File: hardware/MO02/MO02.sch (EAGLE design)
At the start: 28 parts, among them J1 AUDIO-JACK2PTH, J2 M04X2, Q1 G2XX3---PW20, Q4 32.768 kHz, SW1 DTS-6

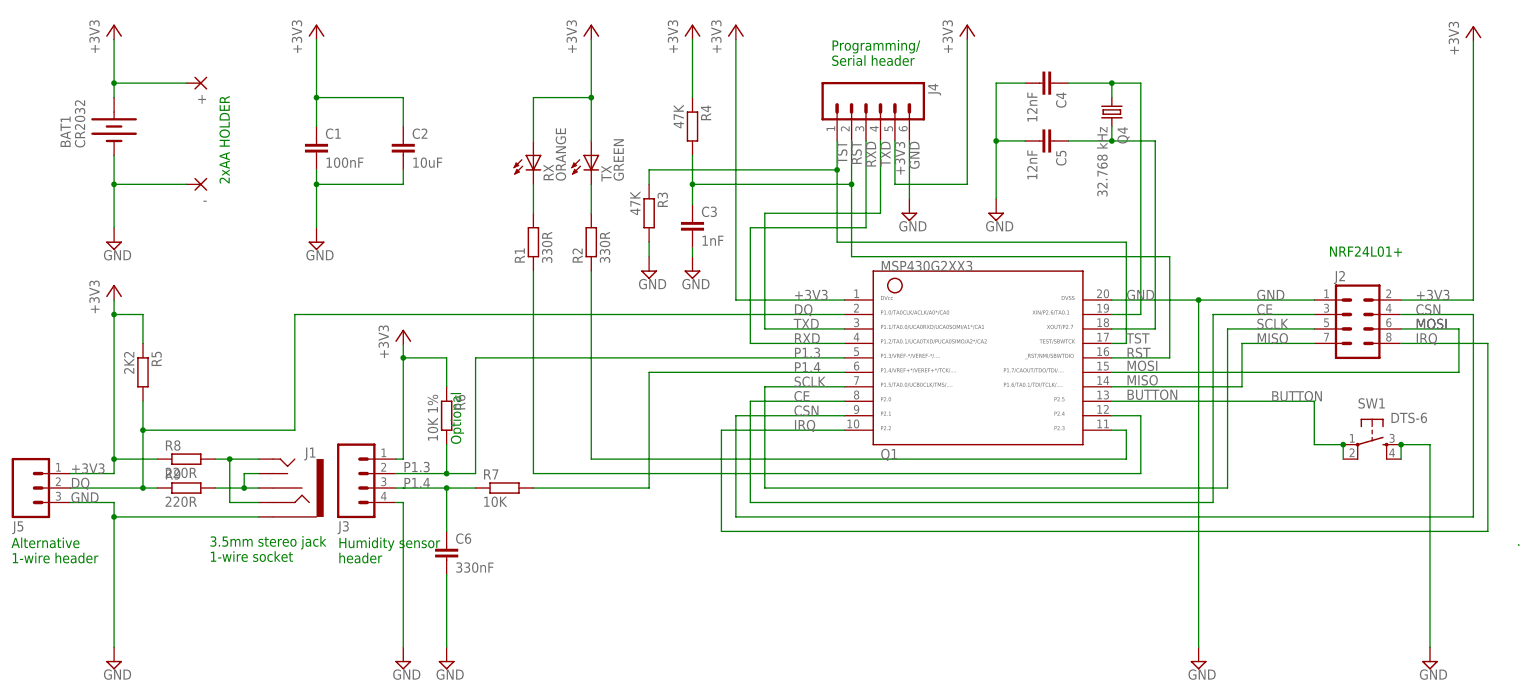
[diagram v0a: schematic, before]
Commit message: 2x6mm watch crystal, isolated ground plane, no external caps
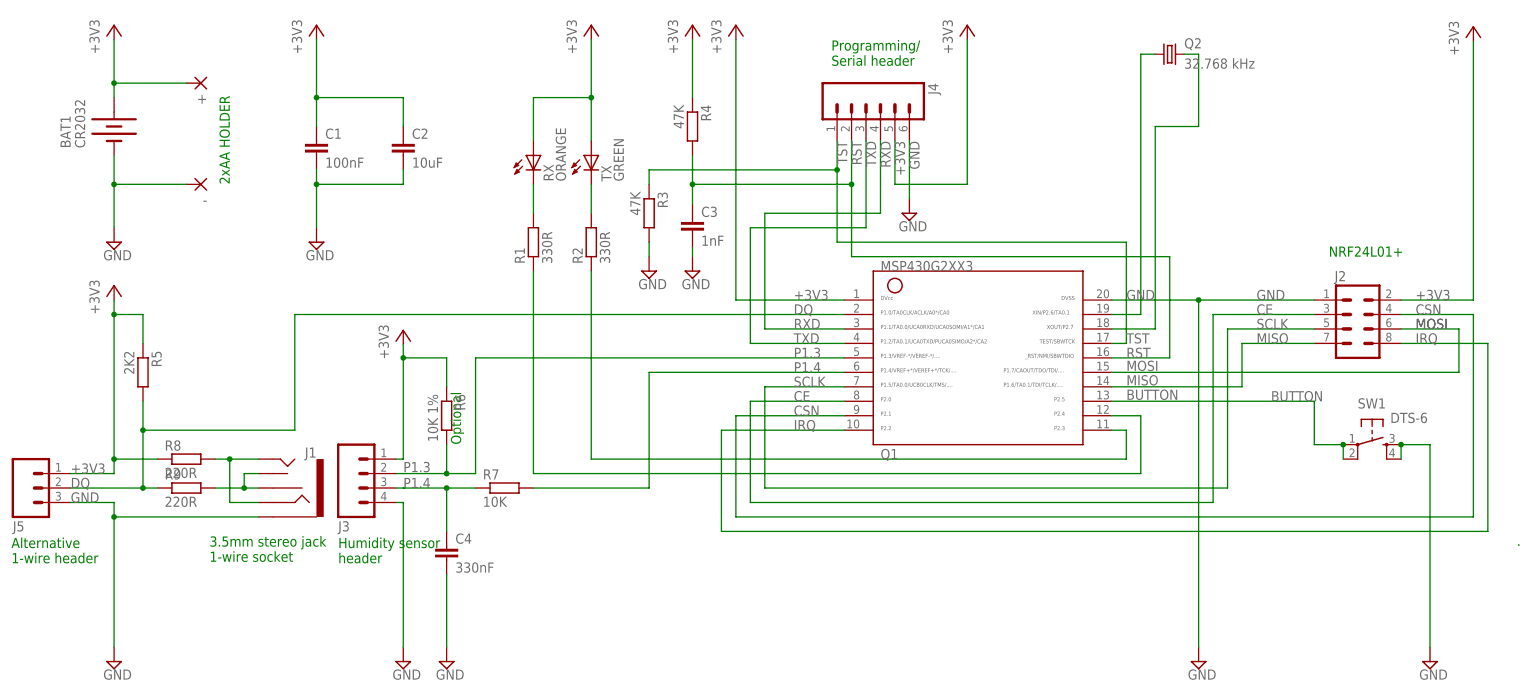
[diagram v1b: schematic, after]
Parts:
- removed C5: 12nF, resistor:C-EUC0805
- removed C6: 330nF, resistor:C-EUC0805
- removed Q4: 32.768 kHz, crystal:CRYSTALTC38H
- added Q2: 32.768 kHz, crystal:CRYSTALTC26H
- C4: value 12nF -> 330nF
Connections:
- net GND: no longer C5.2, C6.2
- net N$7: now also C4.1; no longer C6.1
- net P2.6: now also Q2.1; no longer C4.1, Q4.1
- net P2.7: now also Q2.2; no longer C5.1, Q4.2
- net RXD: now also J4.4, Q1.3; no longer J4.3, Q1.4
- net TXD: now also J4.3, Q1.4; no longer J4.4, Q1.3
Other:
- moved on the sheet: C4
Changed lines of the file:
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@@
 <part name="BAT1" library="SparkFun" deviceset="BATTERY" device="20PTH" value="CR2032"/>
 <part name="Q1" library="TI_MSP430_v16" deviceset="G2XX3---PW20" device=""/>
-<part name="Q4" library="crystal" deviceset="CRYSTAL" device="TC38H" value="32.768 kHz"/>
+<part name="Q2" library="crystal" deviceset="CRYSTAL" device="TC26H" value="32.768 kHz"/>
 <part name="J3" library="SparkFun" deviceset="M04" device="PTH"/>
 <part name="GND4" library="supply2" deviceset="GND" device=""/>
@@
 <attribute name="RESISTANCE" value="4K7"/>
 </part>
-<part name="C4" library="resistor" deviceset="C-EU" device="C0805" value="12nF"/>
-<part name="C5" library="resistor" deviceset="C-EU" device="C0805" value="12nF"/>
-<part name="GND7" library="supply2" deviceset="GND" device=""/>
 <part name="GND8" library="supply2" deviceset="GND" device=""/>
 <part name="C3" library="resistor" deviceset="C-EU" device="C0805" value="1nF"/>
@@
 <part name="+" library="wirepad" deviceset="2,54/1,0" device=""/>
 <part name="GND10" library="supply2" deviceset="GND" device=""/>
-<part name="C6" library="resistor" deviceset="C-EU" device="C0805" value="330nF"/>
+<part name="C4" library="resistor" deviceset="C-EU" device="C0805" value="330nF"/>
 <part name="R7" library="resistor" deviceset="R-EU_" device="M0805" value="10K">
 <attribute name="RESISTANCE" value="4K7"/>
@@
 <attribute name="NAME" x="167.64" y="63.5" size="1.778" layer="95"/>
 </instance>
-<instance part="Q4" gate="G$1" x="208.28" y="124.46" rot="R270"/>
+<instance part="Q2" gate="G$1" x="218.44" y="134.62"/>
 <instance part="J3" gate="G$1" x="77.47" y="60.96" rot="MR180"/>
 <instance part="GND4" gate="GND" x="83.82" y="27.94"/>
@@
 <instance part="P+8" gate="G$1" x="33.02" y="93.98"/>
 <instance part="R5" gate="G$1" x="38.1" y="78.74" rot="R270"/>
-<instance part="C4" gate="G$1" x="198.12" y="129.54" rot="R270"/>
-<instance part="C5" gate="G$1" x="198.12" y="119.38" rot="R270"/>
-<instance part="GND7" gate="GND" x="187.96" y="106.68"/>
 <instance part="GND8" gate="GND" x="134.62" y="96.52"/>
 <instance part="C3" gate="G$1" x="134.62" y="105.664"/>
@@
 <instance part="+" gate="P" x="48.26" y="129.54" rot="R180"/>
 <instance part="GND10" gate="GND" x="91.44" y="27.94"/>
-<instance part="C6" gate="G$1" x="91.44" y="48.26"/>
+<instance part="C4" gate="G$1" x="91.44" y="48.26"/>
 <instance part="R7" gate="G$1" x="101.6" y="58.42"/>
 <instance part="GND2" gate="GND" x="264.16" y="27.94"/>
@@
 </segment>
 </net>
-<net name="RXD" class="0">
+<net name="TXD" class="0">
 <segment>
 <wire x1="161.29" y1="83.82" x2="144.78" y2="83.82" width="0.1524" layer="91"/>
@@
 </segment>
 </net>
-<net name="TXD" class="0">
+<net name="RXD" class="0">
 <segment>
 <wire x1="161.29" y1="86.36" x2="147.32" y2="86.36" width="0.1524" layer="91"/>
@@
 <pinref part="Q1" gate="G$1" pin="19"/>
 <wire x1="208.28" y1="88.9" x2="213.36" y2="88.9" width="0.1524" layer="91"/>
-<wire x1="213.36" y1="88.9" x2="213.36" y2="129.54" width="0.1524" layer="91"/>
-<pinref part="C4" gate="G$1" pin="1"/>
-<pinref part="Q4" gate="G$1" pin="1"/>
-<wire x1="208.28" y1="127" x2="208.28" y2="129.54" width="0.1524" layer="91"/>
-<wire x1="200.66" y1="129.54" x2="208.28" y2="129.54" width="0.1524" layer="91"/>
-<junction x="208.28" y="129.54"/>
-<wire x1="208.28" y1="129.54" x2="213.36" y2="129.54" width="0.1524" layer="91"/>
+<wire x1="213.36" y1="88.9" x2="213.36" y2="134.62" width="0.1524" layer="91"/>
+<pinref part="Q2" gate="G$1" pin="1"/>
+<wire x1="215.9" y1="134.62" x2="213.36" y2="134.62" width="0.1524" layer="91"/>
 </segment>
 </net>
@@
 <pinref part="Q1" gate="G$1" pin="18"/>
 <wire x1="208.28" y1="86.36" x2="215.9" y2="86.36" width="0.1524" layer="91"/>
-<wire x1="215.9" y1="86.36" x2="215.9" y2="119.38" width="0.1524" layer="91"/>
-<wire x1="200.66" y1="119.38" x2="208.28" y2="119.38" width="0.1524" layer="91"/>
-<pinref part="C5" gate="G$1" pin="1"/>
-<pinref part="Q4" gate="G$1" pin="2"/>
-<wire x1="208.28" y1="119.38" x2="215.9" y2="119.38" width="0.1524" layer="91"/>
-<wire x1="208.28" y1="121.92" x2="208.28" y2="119.38" width="0.1524" layer="91"/>
-<junction x="208.28" y="119.38"/>
+<wire x1="215.9" y1="86.36" x2="215.9" y2="121.92" width="0.1524" layer="91"/>
+<pinref part="Q2" gate="G$1" pin="2"/>
+<wire x1="223.52" y1="121.92" x2="215.9" y2="121.92" width="0.1524" layer="91"/>
+<wire x1="220.98" y1="134.62" x2="223.52" y2="134.62" width="0.1524" layer="91"/>
+<wire x1="223.52" y1="134.62" x2="223.52" y2="121.92" width="0.1524" layer="91"/>
 </segment>
 </net>
@@
 </segment>
 <segment>
-<pinref part="C6" gate="G$1" pin="2"/>
+<pinref part="C4" gate="G$1" pin="2"/>
 <pinref part="GND10" gate="GND" pin="GND"/>
 <wire x1="91.44" y1="43.18" x2="91.44" y2="30.48" width="0.1524" layer="91"/>
@@
 </segment>
 <segment>
-<pinref part="GND7" gate="GND" pin="GND"/>
-<wire x1="187.96" y1="109.22" x2="187.96" y2="119.38" width="0.1524" layer="91"/>
-<wire x1="187.96" y1="119.38" x2="187.96" y2="129.54" width="0.1524" layer="91"/>
-<junction x="187.96" y="119.38"/>
-<pinref part="C4" gate="G$1" pin="2"/>
-<wire x1="193.04" y1="129.54" x2="187.96" y2="129.54" width="0.1524" layer="91"/>
-<pinref part="C5" gate="G$1" pin="2"/>
-<wire x1="193.04" y1="119.38" x2="187.96" y2="119.38" width="0.1524" layer="91"/>
-</segment>
-<segment>
 <pinref part="GND8" gate="GND" pin="GND"/>
 <wire x1="134.62" y1="99.06" x2="134.62" y2="100.584" width="0.1524" layer="91"/>
@@
 <net name="N$7" class="0">
 <segment>
-<pinref part="C6" gate="G$1" pin="1"/>
+<pinref part="C4" gate="G$1" pin="1"/>
 <wire x1="91.44" y1="58.42" x2="91.44" y2="50.8" width="0.1524" layer="91"/>
 <pinref part="R7" gate="G$1" pin="1"/>

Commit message: removed pulldown resistor on TST
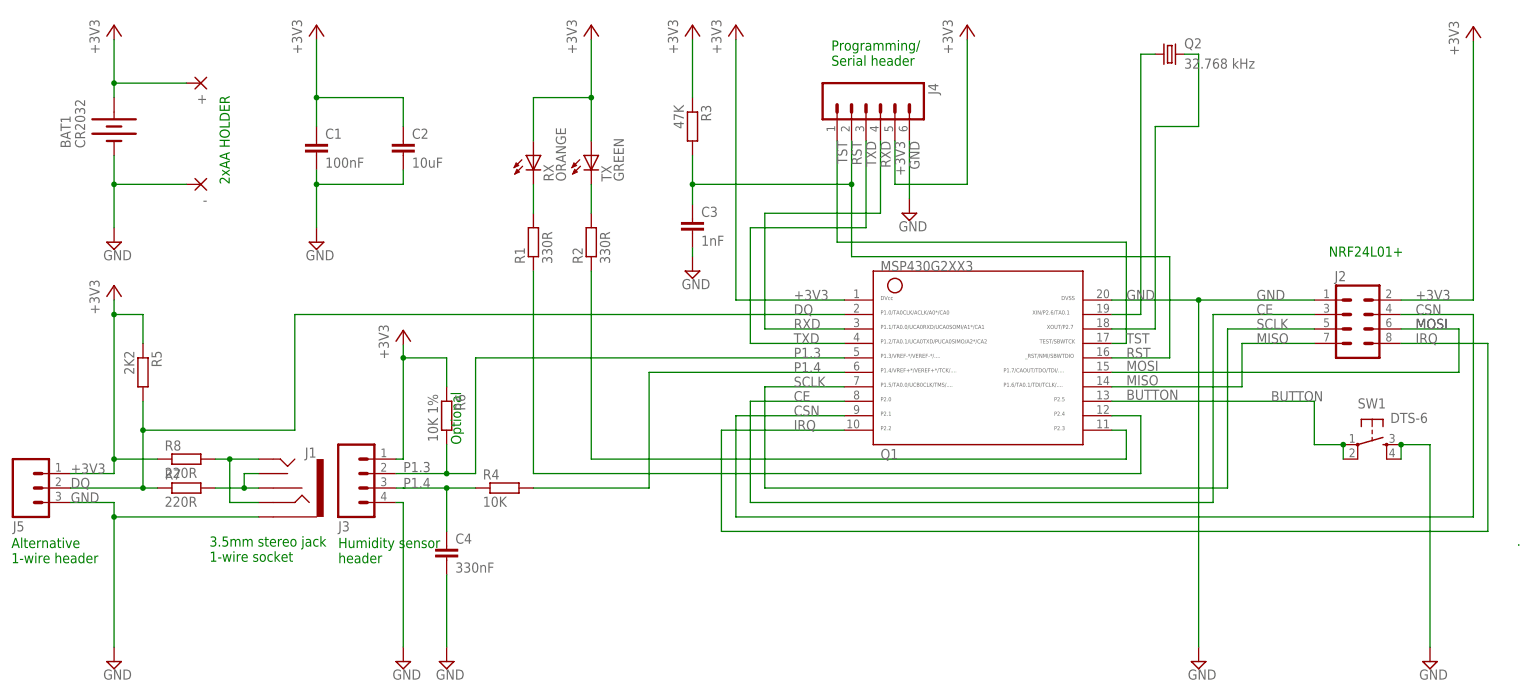
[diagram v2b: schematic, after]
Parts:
- removed R9: 220R, resistor:R-EU_M0805
- R4: value 47K -> 10K
- R7: value 10K -> 220R
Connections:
- net +3V3: now also R3.1; no longer R4.1
- net DQ: now also R7.1; no longer R9.1
- net GND: no longer R3.2
- net N$4: now also R7.2; no longer R9.2
- net N$7: now also R4.1; no longer R7.1
- net P1.4: now also R4.2; no longer R7.2
- net RST: now also R3.2; no longer R4.2
- net TST: no longer R3.1
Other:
- moved on the sheet: R3, R4, R7
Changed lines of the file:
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@@
 <part name="C3" library="resistor" deviceset="C-EU" device="C0805" value="1nF"/>
 <part name="P+10" library="supply1" deviceset="+3V3" device=""/>
-<part name="R4" library="resistor" deviceset="R-EU_" device="M0805" value="47K">
+<part name="R3" library="resistor" deviceset="R-EU_" device="M0805" value="47K">
 <attribute name="RESISTANCE" value="4K7"/>
 </part>
@@
 <part name="SW1" library="switch-tact" deviceset="DTS-6" device=""/>
 <part name="GND3" library="supply2" deviceset="GND" device=""/>
-<part name="R3" library="resistor" deviceset="R-EU_" device="M0805" value="47K">
-<attribute name="RESISTANCE" value="4K7"/>
-</part>
-<part name="GND9" library="supply2" deviceset="GND" device=""/>
 <part name="-" library="wirepad" deviceset="2,54/1,0" device=""/>
 <part name="+" library="wirepad" deviceset="2,54/1,0" device=""/>
 <part name="GND10" library="supply2" deviceset="GND" device=""/>
 <part name="C4" library="resistor" deviceset="C-EU" device="C0805" value="330nF"/>
-<part name="R7" library="resistor" deviceset="R-EU_" device="M0805" value="10K">
+<part name="R4" library="resistor" deviceset="R-EU_" device="M0805" value="10K">
 <attribute name="RESISTANCE" value="4K7"/>
 </part>
@@
 <attribute name="RESISTANCE" value="4K7"/>
 </part>
-<part name="R9" library="resistor" deviceset="R-EU_" device="M0805" value="220R">
+<part name="R7" library="resistor" deviceset="R-EU_" device="M0805" value="220R">
 <attribute name="RESISTANCE" value="4K7"/>
 </part>
@@
 <instance part="C3" gate="G$1" x="134.62" y="105.664"/>
 <instance part="P+10" gate="G$1" x="134.62" y="139.7"/>
-<instance part="R4" gate="G$1" x="134.62" y="121.92" rot="R270"/>
+<instance part="R3" gate="G$1" x="134.62" y="121.92" rot="R270"/>
 <instance part="J4" gate="G$1" x="165.1" y="124.46" rot="R270"/>
 <instance part="P+11" gate="G$1" x="182.88" y="139.7"/>
@@
 <instance part="SW1" gate="G$1" x="254" y="66.04" rot="R270"/>
 <instance part="GND3" gate="GND" x="33.02" y="101.6"/>
-<instance part="R3" gate="G$1" x="127" y="106.68" rot="R270"/>
-<instance part="GND9" gate="GND" x="127" y="96.52"/>
 <instance part="-" gate="P" x="48.26" y="111.76" rot="R180"/>
 <instance part="+" gate="P" x="48.26" y="129.54" rot="R180"/>
 <instance part="GND10" gate="GND" x="91.44" y="27.94"/>
 <instance part="C4" gate="G$1" x="91.44" y="48.26"/>
-<instance part="R7" gate="G$1" x="101.6" y="58.42"/>
+<instance part="R4" gate="G$1" x="101.6" y="58.42"/>
 <instance part="GND2" gate="GND" x="264.16" y="27.94"/>
 <instance part="R8" gate="G$1" x="45.72" y="63.5"/>
-<instance part="R9" gate="G$1" x="45.72" y="58.42"/>
+<instance part="R7" gate="G$1" x="45.72" y="58.42"/>
 </instances>
 <busses>
@@
 <wire x1="64.77" y1="88.9" x2="64.77" y2="68.58" width="0.1524" layer="91"/>
 <label x="152.4" y="88.9" size="1.778" layer="95"/>
-<pinref part="R9" gate="G$1" pin="1"/>
+<pinref part="R7" gate="G$1" pin="1"/>
 <pinref part="J5" gate="G$1" pin="2"/>
 <wire x1="40.64" y1="58.42" x2="38.1" y2="58.42" width="0.1524" layer="91"/>
@@
 <segment>
 <pinref part="P+10" gate="G$1" pin="+3V3"/>
-<pinref part="R4" gate="G$1" pin="1"/>
+<pinref part="R3" gate="G$1" pin="1"/>
 <wire x1="134.62" y1="137.16" x2="134.62" y2="127" width="0.1524" layer="91"/>
 </segment>
@@
 <label x="162.56" y="119.38" size="1.778" layer="95" rot="R270"/>
 <label x="210.82" y="81.28" size="1.778" layer="95"/>
-<pinref part="R4" gate="G$1" pin="2"/>
+<pinref part="R3" gate="G$1" pin="2"/>
 <wire x1="162.56" y1="111.76" x2="134.62" y2="111.76" width="0.1524" layer="91"/>
 <wire x1="134.62" y1="111.76" x2="134.62" y2="116.84" width="0.1524" layer="91"/>
@@
 <pinref part="J4" gate="G$1" pin="1"/>
 <wire x1="210.82" y1="101.6" x2="160.02" y2="101.6" width="0.1524" layer="91"/>
-<wire x1="160.02" y1="101.6" x2="160.02" y2="114.3" width="0.1524" layer="91"/>
+<wire x1="160.02" y1="101.6" x2="160.02" y2="119.38" width="0.1524" layer="91"/>
 <label x="210.82" y="83.82" size="1.778" layer="95"/>
 <label x="160.02" y="119.38" size="1.778" layer="95" rot="R270"/>
-<pinref part="R3" gate="G$1" pin="1"/>
-<wire x1="160.02" y1="114.3" x2="160.02" y2="119.38" width="0.1524" layer="91"/>
-<wire x1="160.02" y1="114.3" x2="127" y2="114.3" width="0.1524" layer="91"/>
-<wire x1="127" y1="114.3" x2="127" y2="111.76" width="0.1524" layer="91"/>
-<junction x="160.02" y="114.3"/>
 </segment>
 </net>
@@
 <wire x1="127" y1="58.42" x2="127" y2="78.74" width="0.1524" layer="91"/>
 <label x="83.82" y="58.42" size="1.778" layer="95"/>
-<pinref part="R7" gate="G$1" pin="2"/>
+<pinref part="R4" gate="G$1" pin="2"/>
 <wire x1="106.68" y1="58.42" x2="127" y2="58.42" width="0.1524" layer="91"/>
 </segment>
@@
 </segment>
 <segment>
-<pinref part="R3" gate="G$1" pin="2"/>
-<wire x1="127" y1="101.6" x2="127" y2="99.06" width="0.1524" layer="91"/>
-<pinref part="GND9" gate="GND" pin="GND"/>
-</segment>
-<segment>
 <pinref part="SW1" gate="G$1" pin="3"/>
 <pinref part="SW1" gate="G$1" pin="4"/>
@@
 <pinref part="C4" gate="G$1" pin="1"/>
 <wire x1="91.44" y1="58.42" x2="91.44" y2="50.8" width="0.1524" layer="91"/>
-<pinref part="R7" gate="G$1" pin="1"/>
+<pinref part="R4" gate="G$1" pin="1"/>
 <wire x1="96.52" y1="58.42" x2="91.44" y2="58.42" width="0.1524" layer="91"/>
 <junction x="91.44" y="58.42"/>
@@
 <wire x1="58.42" y1="58.42" x2="55.88" y2="58.42" width="0.1524" layer="91"/>
 <wire x1="55.88" y1="58.42" x2="55.88" y2="60.96" width="0.1524" layer="91"/>
-<pinref part="R9" gate="G$1" pin="2"/>
+<pinref part="R7" gate="G$1" pin="2"/>
 <wire x1="55.88" y1="58.42" x2="50.8" y2="58.42" width="0.1524" layer="91"/>
 <junction x="55.88" y="58.42"/>
